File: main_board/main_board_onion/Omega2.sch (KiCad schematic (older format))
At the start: 13 parts

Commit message: Added the ethernet jack and related circuits for Omega2
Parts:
- added C?: 1nF/2KV, symbol Device:C_Small
- added C? (x2): 100nF, symbol Device:C
- added C?: 1uF, symbol Device:C
- added J?: RJ45_Shielded, symbol Connector:RJ45_Shielded
- added R? (x2): 75, symbol Device:R
- added R? (x4): 49.9, symbol Device:R
- added U?: H1102, symbol Pulse:H1102
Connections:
- net labels added: RX+, RX-, TX+, TX-
- wire segments 57 -> 119
- no-connect marks 13 -> 21
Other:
- note added: "Ethernet Jack and Magnetic Transformer"
- moved on the sheet: O?

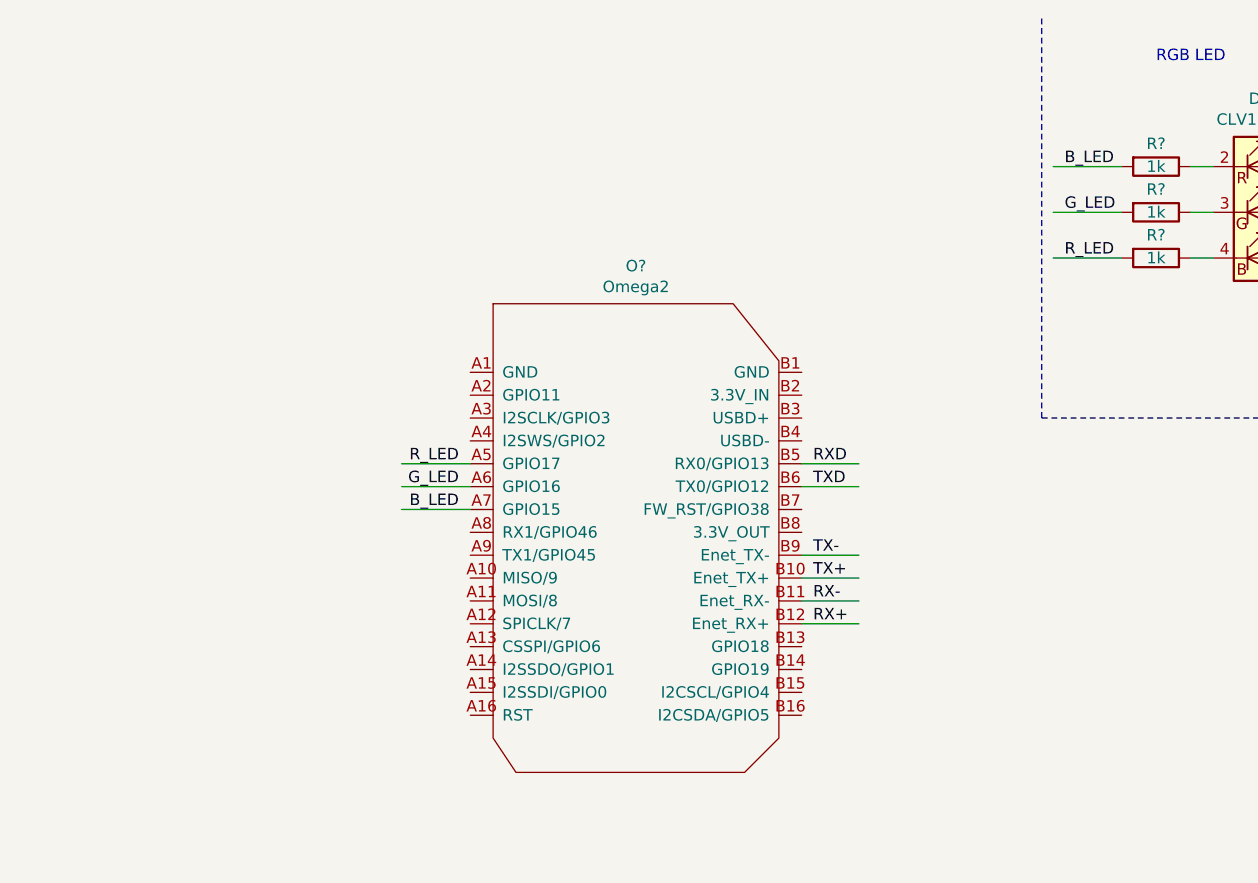
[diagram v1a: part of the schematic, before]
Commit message: Added 24V power, communication between Omega and NXP and Finished ethernet
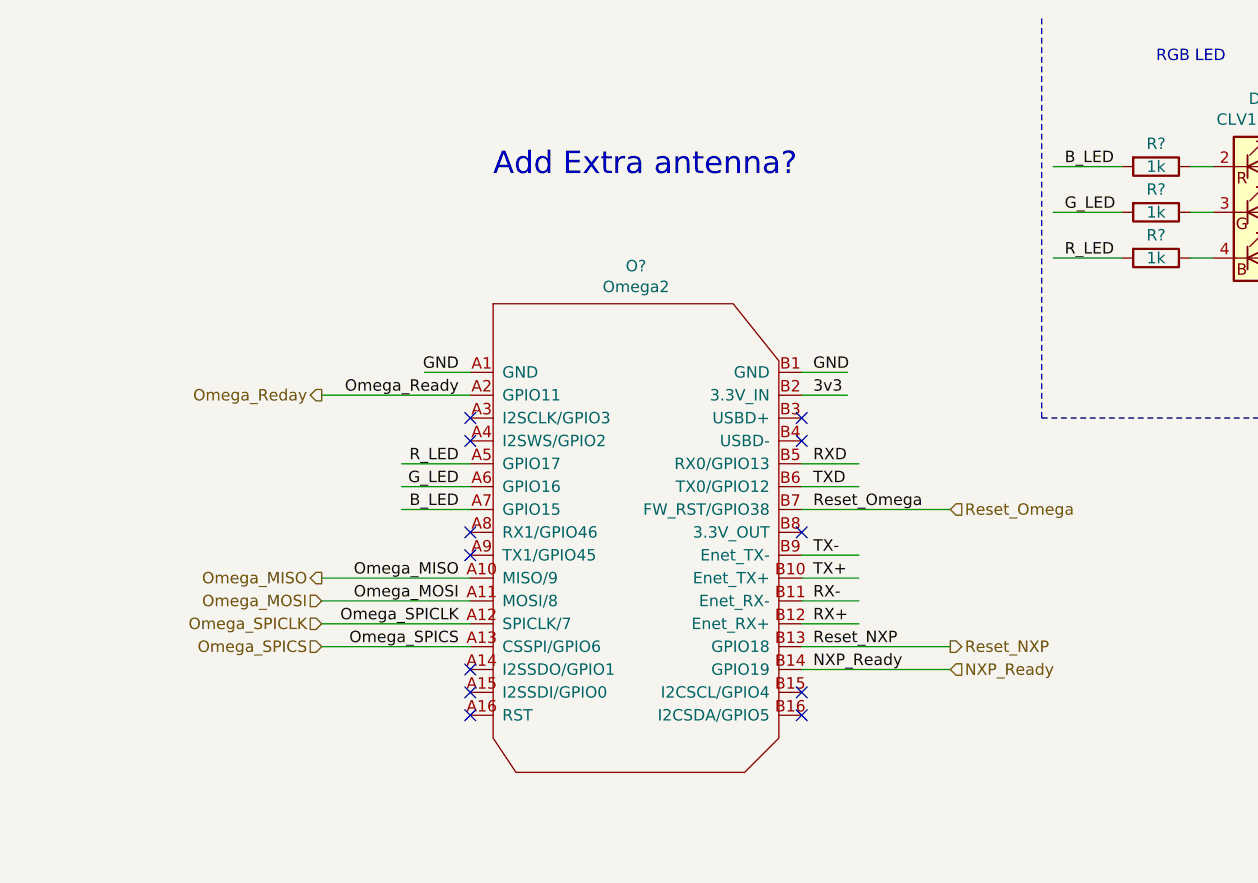
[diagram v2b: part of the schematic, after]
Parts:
- J?: footprint (none) -> TE:1-338088-3
- O?: footprint (none) -> Onion:Omega2p
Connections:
- net labels added: NXP_Ready, Omega_MISO, Omega_MOSI, Omega_Ready, Omega_Reday, Omega_SPICLK, Omega_SPICS, Reset_NXP, Reset_Omega
- wire segments 119 -> 130
- no-connect marks 21 -> 33
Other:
- note added: "Add Extra antenna?"
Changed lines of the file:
@@
 F 0 "O?" H 5725 4015 50  0000 C CNN
 F 1 "Omega2" H 5725 3924 50  0000 C CNN
-F 2 "" H 5300 3150 50  0001 C CNN
+F 2 "Onion:Omega2p" H 5300 3150 50  0001 C CNN
 F 3 "" H 5300 3150 50  0001 C CNN
 	1    5700 2800
@@
 F 0 "J?" H 5221 6298 50  0000 R CNN
 F 1 "RJ45_Shielded" H 5221 6389 50  0000 R CNN
-F 2 "" V 5550 6375 50  0001 C CNN
-F 3 "~" V 5550 6375 50  0001 C CNN
+F 2 "TE:1-338088-3" V 5550 6375 50  0001 C CNN
+F 3 "http://www.te.com/commerce/DocumentDelivery/DDEController?Action=srchrtrv&DocNm=338088&DocType=Customer+Drawing&DocLang=English" V 5550 6375 50  0001 C CNN
 	1    5550 6350
 	-1   0    0    1
@@
 Text Notes 4250 5100 0    50   ~ 0
 Ethernet Jack and Magnetic Transformer
+Text Label 6500 2050 0    50   ~ 0
+GND
+Text Label 4950 2050 2    50   ~ 0
+GND
+Text Label 6500 2150 0    50   ~ 0
+3v3
+Wire Wire Line
+	6450 2150 6650 2150
+Wire Wire Line
+	6450 2050 6650 2050
+Wire Wire Line
+	5000 2050 4800 2050
+Text Label 6500 2650 0    50   ~ 0
+Reset_Omega
+Text Label 4950 2950 2    50   ~ 0
+Omega_MISO
+Text Label 4950 3050 2    50   ~ 0
+Omega_MOSI
+Text Label 4950 3150 2    50   ~ 0
+Omega_SPICLK
+Wire Wire Line
+	5000 3150 4350 3150
+Wire Wire Line
+	5000 3050 4350 3050
+Wire Wire Line
+	5000 2950 4350 2950
+Text Label 4950 3250 2    50   ~ 0
+Omega_SPICS
+Wire Wire Line
+	5000 3250 4350 3250
+NoConn ~ 6450 2250
+NoConn ~ 6450 2350
+NoConn ~ 6450 2750
+NoConn ~ 5000 3550
+Text Label 6500 3250 0    50   ~ 0
+Reset_NXP
+Text Label 6500 3350 0    50   ~ 0
+NXP_Ready
+Wire Wire Line
+	6450 3250 7100 3250
+Wire Wire Line
+	6450 3350 7100 3350
+Text Label 4950 2150 2    50   ~ 0
+Omega_Ready
+NoConn ~ 5000 2250
+NoConn ~ 5000 2350
+NoConn ~ 5000 2750
+NoConn ~ 5000 2850
+NoConn ~ 5000 3350
+NoConn ~ 5000 3450
+NoConn ~ 6450 3450
+NoConn ~ 6450 3550
+Text HLabel 4350 2950 0    50   Output ~ 0
+Omega_MISO
+Text HLabel 4350 3050 0    50   Input ~ 0
+Omega_MOSI
+Text HLabel 4350 3150 0    50   Input ~ 0
+Omega_SPICLK
+Text HLabel 4350 3250 0    50   Input ~ 0
+Omega_SPICS
+Text HLabel 4350 2150 0    50   Output ~ 0
+Omega_Reday
+Wire Wire Line
+	4350 2150 5000 2150
+Text HLabel 7100 2650 2    50   Input ~ 0
+Reset_Omega
+Wire Wire Line
+	6450 2650 7100 2650
+Text HLabel 7100 3350 2    50   Input ~ 0
+NXP_Ready
+Text HLabel 7100 3250 2    50   Output ~ 0
+Reset_NXP
+Text Notes 5100 1200 0    98   ~ 0
+Add Extra antenna?
 $EndSCHEMATC

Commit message: Linked all schematic symbols to appropriate PCB footprints
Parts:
- C15, C16, C17, C18, C19, C20: renamed from C?; footprint (none) -> Capacitor_SMD:C_0603_1608Metric
- J17: renamed from J?; footprint (none) -> Connector_USB:USB_Micro-B_Molex-105017-0001
- R10, R11, R12, R13, R14, R15, R16, R17, R18, R19, R20, R21: renamed from R?; footprint (none) -> Resistor_SMD:R_0603_1608Metric
- U4: renamed from U?; footprint (none) -> Inductor_SMD:L_Coilcraft_XxL4040
- gave numbers to parts that had none: 5
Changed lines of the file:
@@
 $EndDescr
 $Comp
-L Onion:Omega2 O?
+L Onion:Omega2 O1
 U 1 1 5B63412D
 P 5700 2800
-F 0 "O?" H 5725 4015 50  0000 C CNN
+F 0 "O1" H 5725 4015 50  0000 C CNN
 F 1 "Omega2" H 5725 3924 50  0000 C CNN
 F 2 "Onion:Omega2p" H 5300 3150 50  0001 C CNN
@@
 5v
 $Comp
-L Connector:USB_B_Micro J?
+L Connector:USB_B_Micro J17
 U 1 1 5B651845
 P 10650 1200
-F 0 "J?" H 10420 1098 50  0000 R CNN
+F 0 "J17" H 10420 1098 50  0000 R CNN
 F 1 "USB_B_Micro_Omega" H 10900 1550 50  0000 R CNN
-F 2 "" H 10800 1150 50  0001 C CNN
+F 2 "Connector_USB:USB_Micro-B_Molex-105017-0001" H 10800 1150 50  0001 C CNN
 F 3 "~" H 10800 1150 50  0001 C CNN
 	1    10650 1200
@@
 USB Micro Omega w/ serial
 $Comp
-L Interface_USB:CP2102N-A01-GQFN24 U?
+L Interface_USB:CP2102N-A01-GQFN24 U5
 U 1 1 5B651CFD
 P 10100 3500
-F 0 "U?" H 9700 4300 50  0000 C CNN
+F 0 "U5" H 9700 4300 50  0000 C CNN
 F 1 "CP2102N-A01-GQFN24" H 10700 2700 50  0000 C CNN
 F 2 "Package_DFN_QFN:QFN-24-1EP_4x4mm_P0.5mm_EP2.6x2.6mm" H 10550 2700 50  0001 L CNN
@@
 	9050 3900 9500 3900
 $Comp
-L Device:C_Small C?
+L Device:C_Small C20
 U 1 1 5B652416
 P 9250 3600
-F 0 "C?" H 9300 3650 50  0000 L CNN
+F 0 "C20" H 9300 3650 50  0000 L CNN
 F 1 "4.7uF" H 9250 3500 50  0000 L CNN
-F 2 "" H 9250 3600 50  0001 C CNN
+F 2 "Capacitor_SMD:C_0603_1608Metric" H 9250 3600 50  0001 C CNN
 F 3 "~" H 9250 3600 50  0001 C CNN
 	1    9250 3600
@@
 $EndComp
 $Comp
-L Device:C_Small C?
+L Device:C_Small C19
 U 1 1 5B652450
 P 9050 3600
-F 0 "C?" H 8850 3650 50  0000 L CNN
+F 0 "C19" H 8850 3650 50  0000 L CNN
 F 1 "0.1uF" H 8800 3550 50  0000 L CNN
-F 2 "" H 9050 3600 50  0001 C CNN
+F 2 "Capacitor_SMD:C_0603_1608Metric" H 9050 3600 50  0001 C CNN
 F 3 "~" H 9050 3600 50  0001 C CNN
 	1    9050 3600
@@
 	10000 2500 10000 2600
 $Comp
-L Device:R_Small R?
+L Device:R_Small R19
 U 1 1 5B65310D
 P 9350 2750
-F 0 "R?" H 9409 2796 50  0000 L CNN
+F 0 "R19" H 9409 2796 50  0000 L CNN
 F 1 "1k" H 9409 2705 50  0000 L CNN
-F 2 "" H 9350 2750 50  0001 C CNN
+F 2 "Resistor_SMD:R_0603_1608Metric" H 9350 2750 50  0001 C CNN
 F 3 "~" H 9350 2750 50  0001 C CNN
 	1    9350 2750
@@
 	9600 1500 10150 1500
 $Comp
-L Power_Protection:SP0503BAHT D?
+L Power_Protection:SP0503BAHT D3
 U 1 1 5B66BC75
 P 9550 1200
-F 0 "D?" V 9208 1200 50  0000 C CNN
+F 0 "D3" V 9208 1200 50  0000 C CNN
 F 1 "SP0503BAHT" V 9299 1200 50  0000 C CNN
 F 2 "Package_TO_SOT_SMD:SOT-143" H 9775 1150 50  0001 L CNN
@@
 D+IN_Omega
 $Comp
-L Device:R_Small R?
+L Device:R_Small R20
 U 1 1 5B69A77B
 P 10100 1800
-F 0 "R?" V 9904 1800 50  0000 C CNN
+F 0 "R20" V 9904 1800 50  0000 C CNN
 F 1 "33" V 9995 1800 50  0000 C CNN
-F 2 "" H 10100 1800 50  0001 C CNN
+F 2 "Resistor_SMD:R_0603_1608Metric" H 10100 1800 50  0001 C CNN
 F 3 "~" H 10100 1800 50  0001 C CNN
 	1    10100 1800
@@
 $EndComp
 $Comp
-L Device:R_Small R?
+L Device:R_Small R21
 U 1 1 5B69A7E8
 P 10100 1900
-F 0 "R?" V 10300 1900 50  0000 C CNN
+F 0 "R21" V 10300 1900 50  0000 C CNN
 F 1 "33" V 10200 1900 50  0000 C CNN
-F 2 "" H 10100 1900 50  0001 C CNN
+F 2 "Resistor_SMD:R_0603_1608Metric" H 10100 1900 50  0001 C CNN
 F 3 "~" H 10100 1900 50  0001 C CNN
 	1    10100 1900
@@
 	6450 2550 6700 2550
 $Comp
-L LED:CLV1L-FKB D?
+L LED:CLV1L-FKB D2
 U 1 1 5B6A8E1C
 P 8450 1350
-F 0 "D?" H 8450 1847 50  0000 C CNN
+F 0 "D2" H 8450 1847 50  0000 C CNN
 F 1 "CLV1L-FKB" H 8450 1756 50  0000 C CNN
 F 2 "LED_SMD:LED_Cree-PLCC4_3.2x2.8mm_CCW" H 8450 1300 50  0001 C CNN
@@
 3v3
 $Comp
-L Device:R R?
+L Device:R R16
 U 1 1 5B6AA8B8
 P 8000 1150
-F 0 "R?" V 7900 1150 50  0000 C CNN
+F 0 "R16" V 7900 1150 50  0000 C CNN
 F 1 "1k" V 8000 1150 50  0000 C CNN
-F 2 "" V 7930 1150 50  0001 C CNN
+F 2 "Resistor_SMD:R_0603_1608Metric" V 7930 1150 50  0001 C CNN
 F 3 "~" H 8000 1150 50  0001 C CNN
 	1    8000 1150
@@
 $EndComp
 $Comp
-L Device:R R?
+L Device:R R17
 U 1 1 5B6AA9DD
 P 8000 1350
-F 0 "R?" V 7900 1350 50  0000 C CNN
+F 0 "R17" V 7900 1350 50  0000 C CNN
 F 1 "1k" V 8000 1350 50  0000 C CNN
-F 2 "" V 7930 1350 50  0001 C CNN
+F 2 "Resistor_SMD:R_0603_1608Metric" V 7930 1350 50  0001 C CNN
 F 3 "~" H 8000 1350 50  0001 C CNN
 	1    8000 1350
@@
 $EndComp
 $Comp
-L Device:R R?
+L Device:R R18
 U 1 1 5B6AAA0D
 P 8000 1550
-F 0 "R?" V 7900 1550 50  0000 C CNN
+F 0 "R18" V 7900 1550 50  0000 C CNN
 F 1 "1k" V 8000 1550 50  0000 C CNN
-F 2 "" V 7930 1550 50  0001 C CNN
+F 2 "Resistor_SMD:R_0603_1608Metric" V 7930 1550 50  0001 C CNN
 F 3 "~" H 8000 1550 50  0001 C CNN
 	1    8000 1550
@@
 	7500 2250 11200 2250
 $Comp
-L Pulse:H1102 U?
+L Pulse:H1102 U4
 U 1 1 5B6C2CE9
 P 3100 6450
-F 0 "U?" H 3125 7325 50  0000 C CNN
+F 0 "U4" H 3125 7325 50  0000 C CNN
 F 1 "H1102" H 3125 7234 50  0000 C CNN
-F 2 "" H 2800 6750 50  0001 C CNN
+F 2 "Inductor_SMD:L_Coilcraft_XxL4040" H 2800 6750 50  0001 C CNN
 F 3 "" H 2800 6750 50  0001 C CNN
 	1    3100 6450
@@
 NoConn ~ 2450 7100
 $Comp
-L Connector:RJ45_Shielded J?
+L Connector:RJ45_Shielded J16
 U 1 1 5B6C7EA3
 P 5550 6350
-F 0 "J?" H 5221 6298 50  0000 R CNN
+F 0 "J16" H 5221 6298 50  0000 R CNN
 F 1 "RJ45_Shielded" H 5221 6389 50  0000 R CNN
 F 2 "TE:1-338088-3" V 5550 6375 50  0001 C CNN
@@
 	4300 6900 3800 6900
 $Comp
-L Device:R R?
+L Device:R R14
 U 1 1 5B6CE392
 P 3950 7300
-F 0 "R?" H 4020 7346 50  0000 L CNN
+F 0 "R14" H 4020 7346 50  0000 L CNN
 F 1 "75" H 4020 7255 50  0000 L CNN
-F 2 "" V 3880 7300 50  0001 C CNN
+F 2 "Resistor_SMD:R_0603_1608Metric" V 3880 7300 50  0001 C CNN
 F 3 "~" H 3950 7300 50  0001 C CNN
 	1    3950 7300
@@
 $EndComp
 $Comp
-L Device:R R?
+L Device:R R15
 U 1 1 5B6CE45E
 P 4200 7300
-F 0 "R?" H 4270 7346 50  0000 L CNN
+F 0 "R15" H 4270 7346 50  0000 L CNN
 F 1 "75" H 4270 7255 50  0000 L CNN
-F 2 "" V 4130 7300 50  0001 C CNN
+F 2 "Resistor_SMD:R_0603_1608Metric" V 4130 7300 50  0001 C CNN
 F 3 "~" H 4200 7300 50  0001 C CNN
 	1    4200 7300
@@
 	4200 7600 5000 7600
 $Comp
-L Device:C_Small C?
+L Device:C_Small C18
 U 1 1 5B6D6417
 P 5650 7600
-F 0 "C?" V 5421 7600 50  0000 C CNN
+F 0 "C18" V 5421 7600 50  0000 C CNN
 F 1 "1nF/2KV" V 5512 7600 50  0000 C CNN
-F 2 "" H 5650 7600 50  0001 C CNN
+F 2 "Capacitor_SMD:C_0603_1608Metric" H 5650 7600 50  0001 C CNN
 F 3 "~" H 5650 7600 50  0001 C CNN
 	1    5650 7600
@@
 	5000 5800 5000 7600
 $Comp
-L Device:R R?
+L Device:R R10
 U 1 1 5B6EE2BA
 P 1850 5500
-F 0 "R?" H 1700 5550 50  0000 L CNN
+F 0 "R10" H 1700 5550 50  0000 L CNN
 F 1 "49.9" H 1600 5450 50  0000 L CNN
-F 2 "" V 1780 5500 50  0001 C CNN
+F 2 "Resistor_SMD:R_0603_1608Metric" V 1780 5500 50  0001 C CNN
 F 3 "~" H 1850 5500 50  0001 C CNN
 	1    1850 5500
@@
 $EndComp
 $Comp
-L Device:R R?
+L Device:R R12
 U 1 1 5B6EE3D5
 P 1950 5500
-F 0 "R?" H 2020 5546 50  0000 L CNN
+F 0 "R12" H 2020 5546 50  0000 L CNN
 F 1 "49.9" H 2020 5455 50  0000 L CNN
-F 2 "" V 1880 5500 50  0001 C CNN
+F 2 "Resistor_SMD:R_0603_1608Metric" V 1880 5500 50  0001 C CNN
 F 3 "~" H 1950 5500 50  0001 C CNN
 	1    1950 5500
@@
 $EndComp
 $Comp
-L Device:C C?
+L Device:C C15
 U 1 1 5B6EE44E
 P 1350 5050
-F 0 "C?" V 1098 5050 50  0000 C CNN
+F 0 "C15" V 1098 5050 50  0000 C CNN
 F 1 "100nF" V 1189 5050 50  0000 C CNN
-F 2 "" H 1388 4900 50  0001 C CNN
+F 2 "Capacitor_SMD:C_0603_1608Metric" H 1388 4900 50  0001 C CNN
 F 3 "~" H 1350 5050 50  0001 C CNN
 	1    1350 5050
@@
 	2250 5050 2500 5050
 $Comp
-L Device:C C?
+L Device:C C17
 U 1 1 5B716833
 P 2500 5300
-F 0 "C?" H 2385 5254 50  0000 R CNN
+F 0 "C17" H 2385 5254 50  0000 R CNN
 F 1 "1uF" H 2385 5345 50  0000 R CNN
-F 2 "" H 2538 5150 50  0001 C CNN
+F 2 "Capacitor_SMD:C_0603_1608Metric" H 2538 5150 50  0001 C CNN
 F 3 "~" H 2500 5300 50  0001 C CNN
 	1    2500 5300
@@
 RX+
 $Comp
-L Device:R R?
+L Device:R R11
 U 1 1 5B7228FD
 P 1850 7200
-F 0 "R?" H 1700 7250 50  0000 L CNN
+F 0 "R11" H 1700 7250 50  0000 L CNN
 F 1 "49.9" H 1600 7150 50  0000 L CNN
-F 2 "" V 1780 7200 50  0001 C CNN
+F 2 "Resistor_SMD:R_0603_1608Metric" V 1780 7200 50  0001 C CNN
 F 3 "~" H 1850 7200 50  0001 C CNN
 	1    1850 7200
@@
 $EndComp
 $Comp
-L Device:R R?
+L Device:R R13
 U 1 1 5B722904
 P 1950 7200
-F 0 "R?" H 2020 7246 50  0000 L CNN
+F 0 "R13" H 2020 7246 50  0000 L CNN
 F 1 "49.9" H 2020 7155 50  0000 L CNN
-F 2 "" V 1880 7200 50  0001 C CNN
+F 2 "Resistor_SMD:R_0603_1608Metric" V 1880 7200 50  0001 C CNN
 F 3 "~" H 1950 7200 50  0001 C CNN
 	1    1950 7200
@@
 $EndComp
 $Comp
-L Device:C C?
+L Device:C C16
 U 1 1 5B72290B
 P 1350 7650
-F 0 "C?" V 1602 7650 50  0000 C CNN
+F 0 "C16" V 1602 7650 50  0000 C CNN
 F 1 "100nF" V 1511 7650 50  0000 C CNN
-F 2 "" H 1388 7500 50  0001 C CNN
+F 2 "Capacitor_SMD:C_0603_1608Metric" H 1388 7500 50  0001 C CNN
 F 3 "~" H 1350 7650 50  0001 C CNN
 	1    1350 7650

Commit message: Started Layout
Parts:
- removed J16: RJ45_Shielded, TE:1-338088-3, symbol Connector:RJ45_Shielded
- added J16: RJ45, TE:1-338088-3, symbol Connector:RJ45
- U4: footprint Inductor_SMD:L_Coilcraft_XxL4040 -> Package_SO:SOIC-16W_7.5x12.8mm_P1.27mm
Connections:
- wire segments 130 -> 126
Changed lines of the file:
@@
 Wire Wire Line
 	9500 3800 9500 3500
-Connection ~ 9500 3500
 Text Notes 9600 2350 0    50   ~ 0
 USB to Serial Chip (like FTDI)
@@
 F 0 "U4" H 3125 7325 50  0000 C CNN
 F 1 "H1102" H 3125 7234 50  0000 C CNN
-F 2 "Inductor_SMD:L_Coilcraft_XxL4040" H 2800 6750 50  0001 C CNN
+F 2 "Package_SO:SOIC-16W_7.5x12.8mm_P1.27mm" H 2800 6750 50  0001 C CNN
 F 3 "" H 2800 6750 50  0001 C CNN
 	1    3100 6450
@@
 NoConn ~ 2450 7200
 NoConn ~ 2450 7100
-$Comp
-L Connector:RJ45_Shielded J16
-U 1 1 5B6C7EA3
-P 5550 6350
-F 0 "J16" H 5221 6298 50  0000 R CNN
-F 1 "RJ45_Shielded" H 5221 6389 50  0000 R CNN
-F 2 "TE:1-338088-3" V 5550 6375 50  0001 C CNN
-F 3 "http://www.te.com/commerce/DocumentDelivery/DDEController?Action=srchrtrv&DocNm=338088&DocType=Customer+Drawing&DocLang=English" V 5550 6375 50  0001 C CNN
-	1    5550 6350
-	-1   0    0    1
-$EndComp
 Wire Wire Line
 	5150 6550 4500 6550
@@
 	4200 7450 4200 7600
 Connection ~ 4200 7600
-Wire Wire Line
-	4200 7600 5000 7600
 $Comp
 L Device:C_Small C18
@@
 Text Label 5950 7600 0    50   ~ 0
 GND
-Connection ~ 5000 7600
-Wire Wire Line
-	5000 7600 5550 7600
 NoConn ~ 5150 6350
 NoConn ~ 5150 6450
 NoConn ~ 5150 6650
 NoConn ~ 5150 6750
-Wire Wire Line
-	5550 5850 5550 5800
-Wire Wire Line
-	5550 5800 5000 5800
-Wire Wire Line
-	5000 5800 5000 7600
 $Comp
 L Device:R R10
@@
 Text Notes 5100 1200 0    98   ~ 0
 Add Extra antenna?
+$Comp
+L Connector:RJ45 J16
+U 1 1 5B6A0DFB
+P 5550 6350
+F 0 "J16" H 5220 6354 50  0000 R CNN
+F 1 "RJ45" H 5220 6445 50  0000 R CNN
+F 2 "TE:1-338088-3" V 5550 6375 50  0001 C CNN
+F 3 "http://www.te.com/commerce/DocumentDelivery/DDEController?Action=srchrtrv&DocNm=338088&DocType=Customer+Drawing&DocLang=English" V 5550 6375 50  0001 C CNN
+	1    5550 6350
+	-1   0    0    1
+$EndComp
+Wire Wire Line
+	4200 7600 5550 7600
+Connection ~ 9500 3500
 $EndSCHEMATC

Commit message: Things that I did a long time ago and don't remember what they were....
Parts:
- D3: symbol Power_Protection:SP0503BAHT -> main_board_onion-rescue:SP0503BAHT-Power_Protection
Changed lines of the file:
@@
 	9600 1500 10150 1500
 $Comp
-L Power_Protection:SP0503BAHT D3
+L main_board_onion-rescue:SP0503BAHT-Power_Protection D3
 U 1 1 5B66BC75
 P 9550 1200
